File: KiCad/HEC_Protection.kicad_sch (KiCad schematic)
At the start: 11 parts, among them U10 74LS30, U11 74LS32, U17 74LS74, U18 74LS74, U19 74LS30, U22 74LS02, U23 74LS30, U24 74LS74, U25 74LS541, U26 74LS541

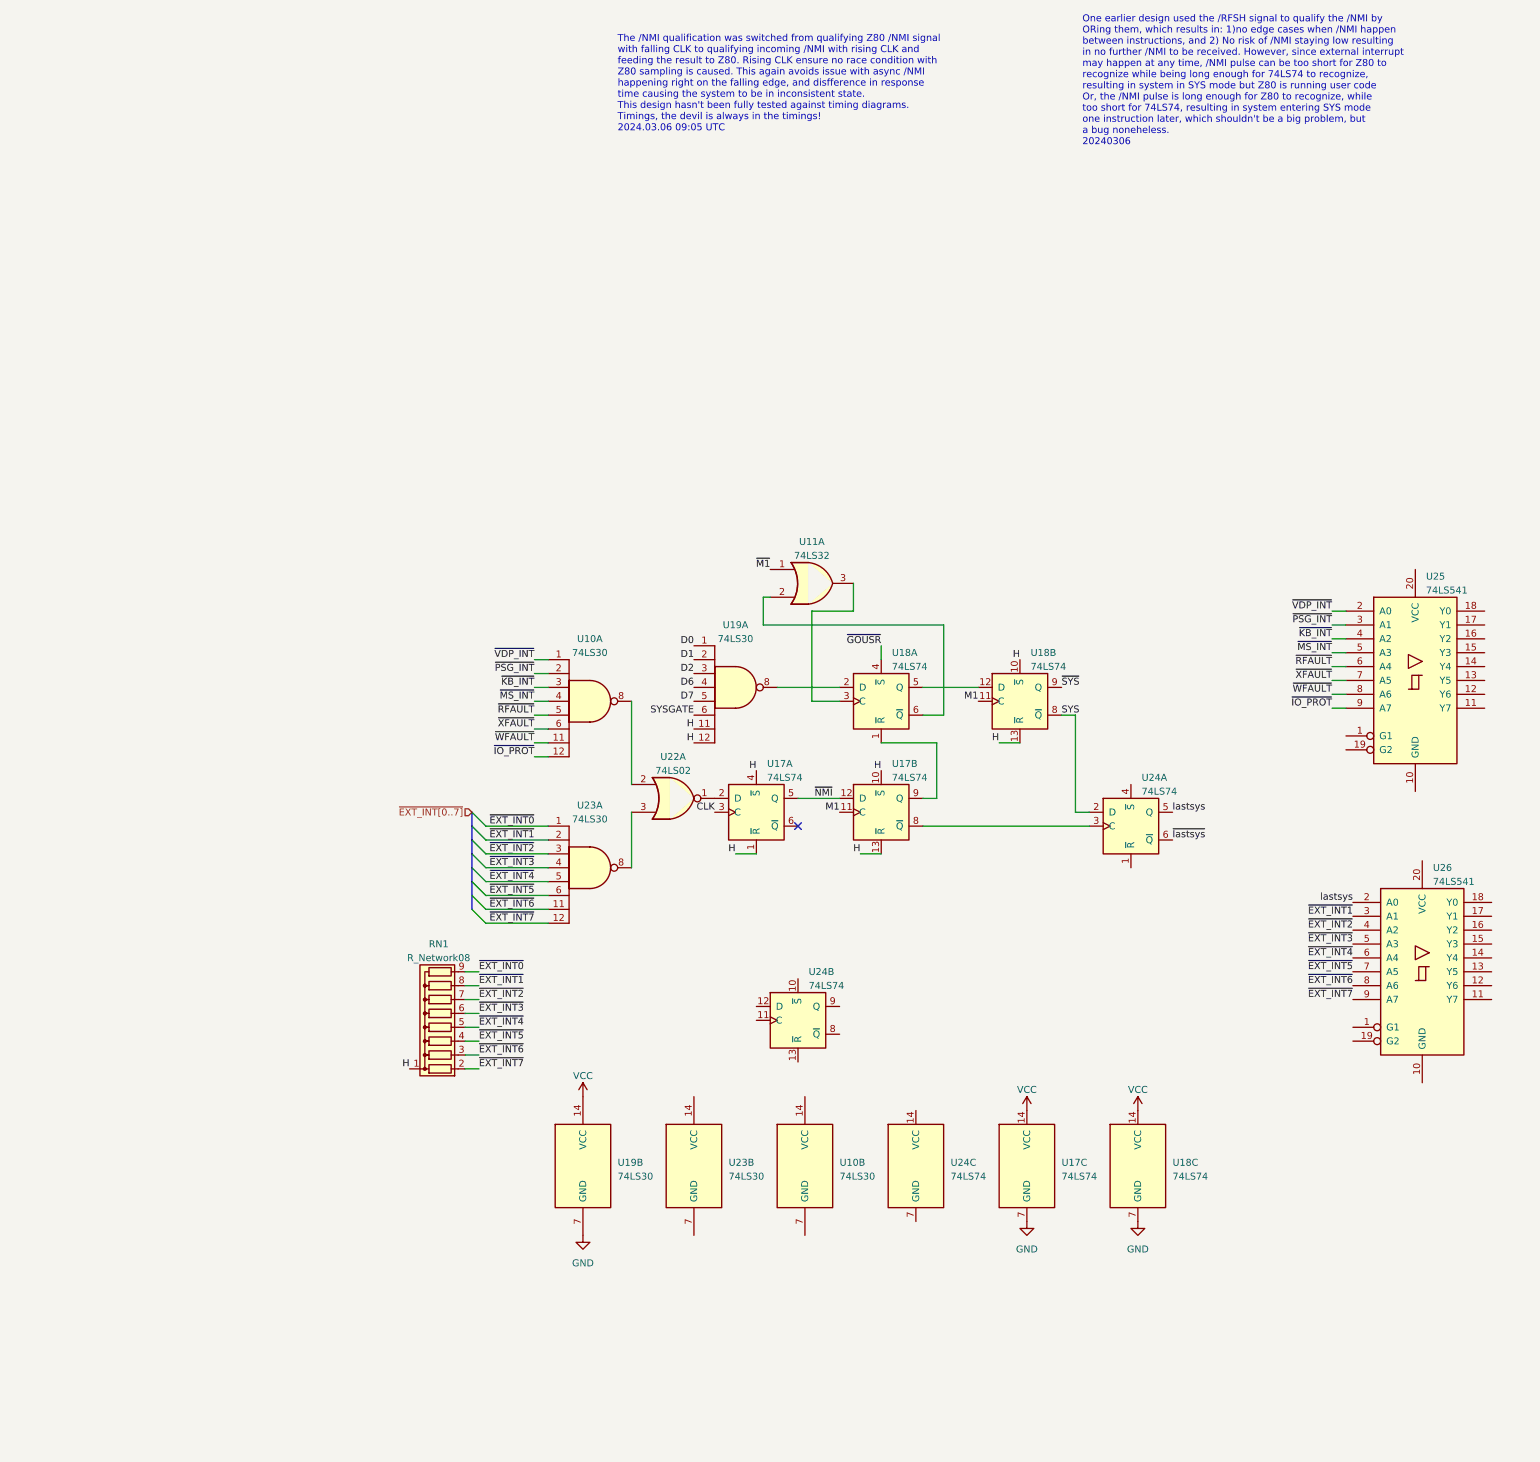
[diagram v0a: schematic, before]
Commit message: Update NMI timing circuit
Updated the NMI generation circuit to prevent a bug occurring when NMI is generated between the rising edge of the last T cycle of an instruction and the falling edge of M1 of the next. Due to delay in M1 signal, the NMI would be qualified one instruction earlier, causing the HEC to enter SYS mode one instruction earlier. If the instruction is an IO instruction by an user program, it can cause a write to any port and potentially destabilize the system.
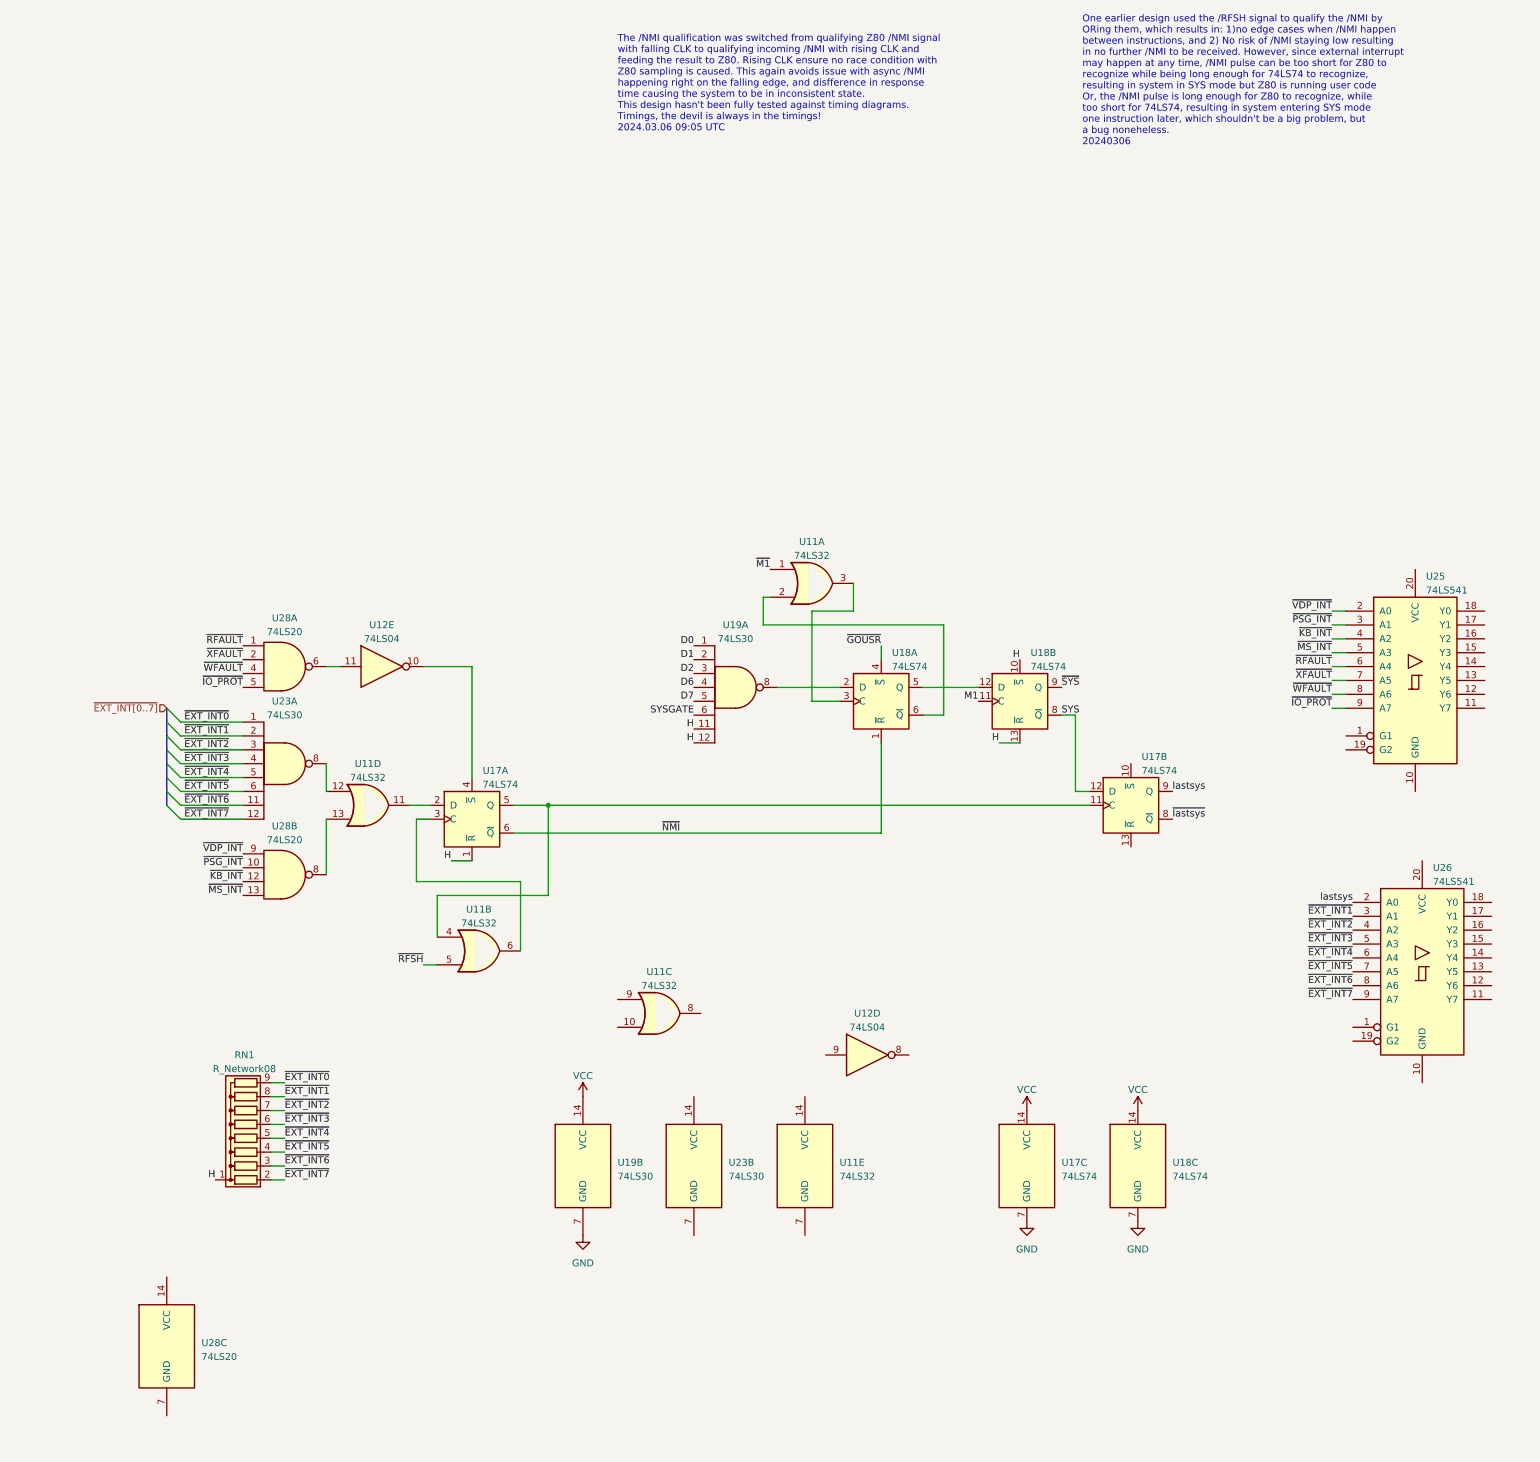
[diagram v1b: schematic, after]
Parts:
- removed U10: 74LS30, Package_DIP:DIP-14_W7.62mm_Socket, symbol 74xx:74LS30
- removed U22: 74LS02, Package_DIP:DIP-14_W7.62mm_Socket, symbol 74xx:74LS02
- removed U24: 74LS74, Package_DIP:DIP-14_W7.62mm_Socket, symbol 74xx:74LS74
- added unit 2 of U11
- added unit 3 of U11
- added unit 4 of U11
- added unit 5 of U11
- added U12: 74LS04, Package_DIP:DIP-14_W7.62mm_Socket, symbol 74xx:74LS04
- added U28: 74LS20, symbol 74xx:74LS20
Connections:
- net H: no longer U17.10 (~{S}), U17.13 (~{R}), U17.4 (~{S})
- net M1: no longer U17.11 (C)
- net SYS: now also U17.12 (D)
- net lastsys: now also U17.9 (Q)
- net ~{IO_PROT}: now also U28.5
- net ~{KB_INT}: now also U28.12
- net ~{MS_INT}: now also U28.13
- net ~{NMI}: now also U17.6 (~{Q}), U18.1 (~{R}); no longer U17.12 (D), U17.5 (Q)
- net ~{PSG_INT}: now also U28.10
- net ~{RFAULT}: now also U28.1
- net ~{VDP_INT}: now also U28.9
- net ~{WFAULT}: now also U28.4
- net ~{XFAULT}: now also U28.2
- net ~{lastsys}: now also U17.8 (~{Q})
- net at U23.8: now also U11.12
- net at U17.2 (D): now also U11.11
- net CLK: no longer names the net of U17.3 (C)
- net CLK: now also U11.6
- new net: U11.4, U17.11 (C), U17.5 (Q)
- new net: U12.10, U17.4 (~{S})
- new net: U12.11, U28.6
- new net: U11.13, U28.8
- new net ~{RFSH}: U11.5
- no-connect marks 1 -> 0
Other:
- moved on the sheet: RN1, U17A, U17B, U23A

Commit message: Add NMI reset circuit
Added a circuit that will reset /NMI state for the HEC and allow further NMI when /INTEN or /GOUSR port is accessed.
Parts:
- added U11: 74LS08, symbol 74xx:74LS08
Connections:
- net H: no longer U17.1 (~{R})
- net ~{GOUSR}: now also U11.1
- new net: U11.3, U17.1 (~{R})
- new net ~{INTEN}: U11.2
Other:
- moved on the sheet: U11A, U19A

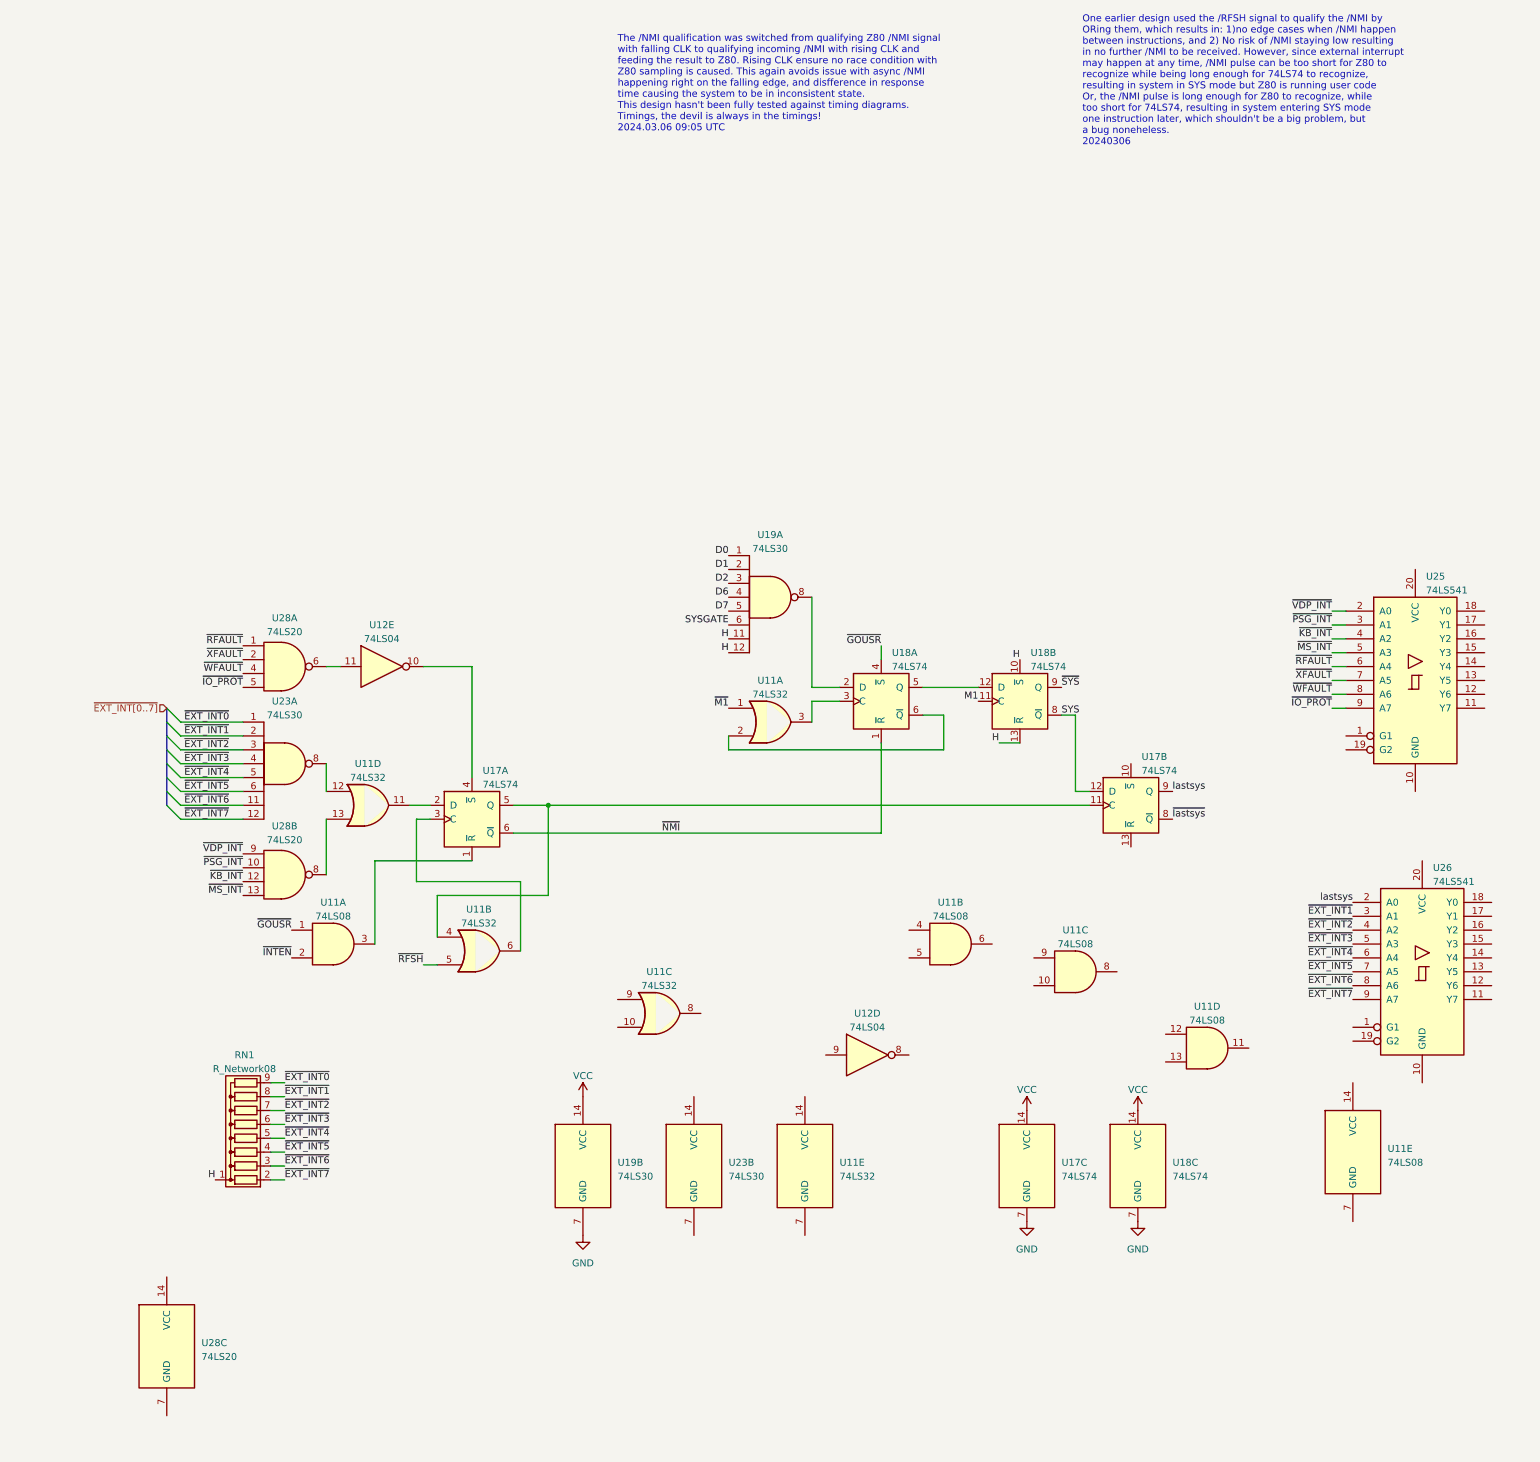
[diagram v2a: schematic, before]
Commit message: Update to protection circuit
Update the protection circuit to prevent all interrupts when HEC is in SYS mode
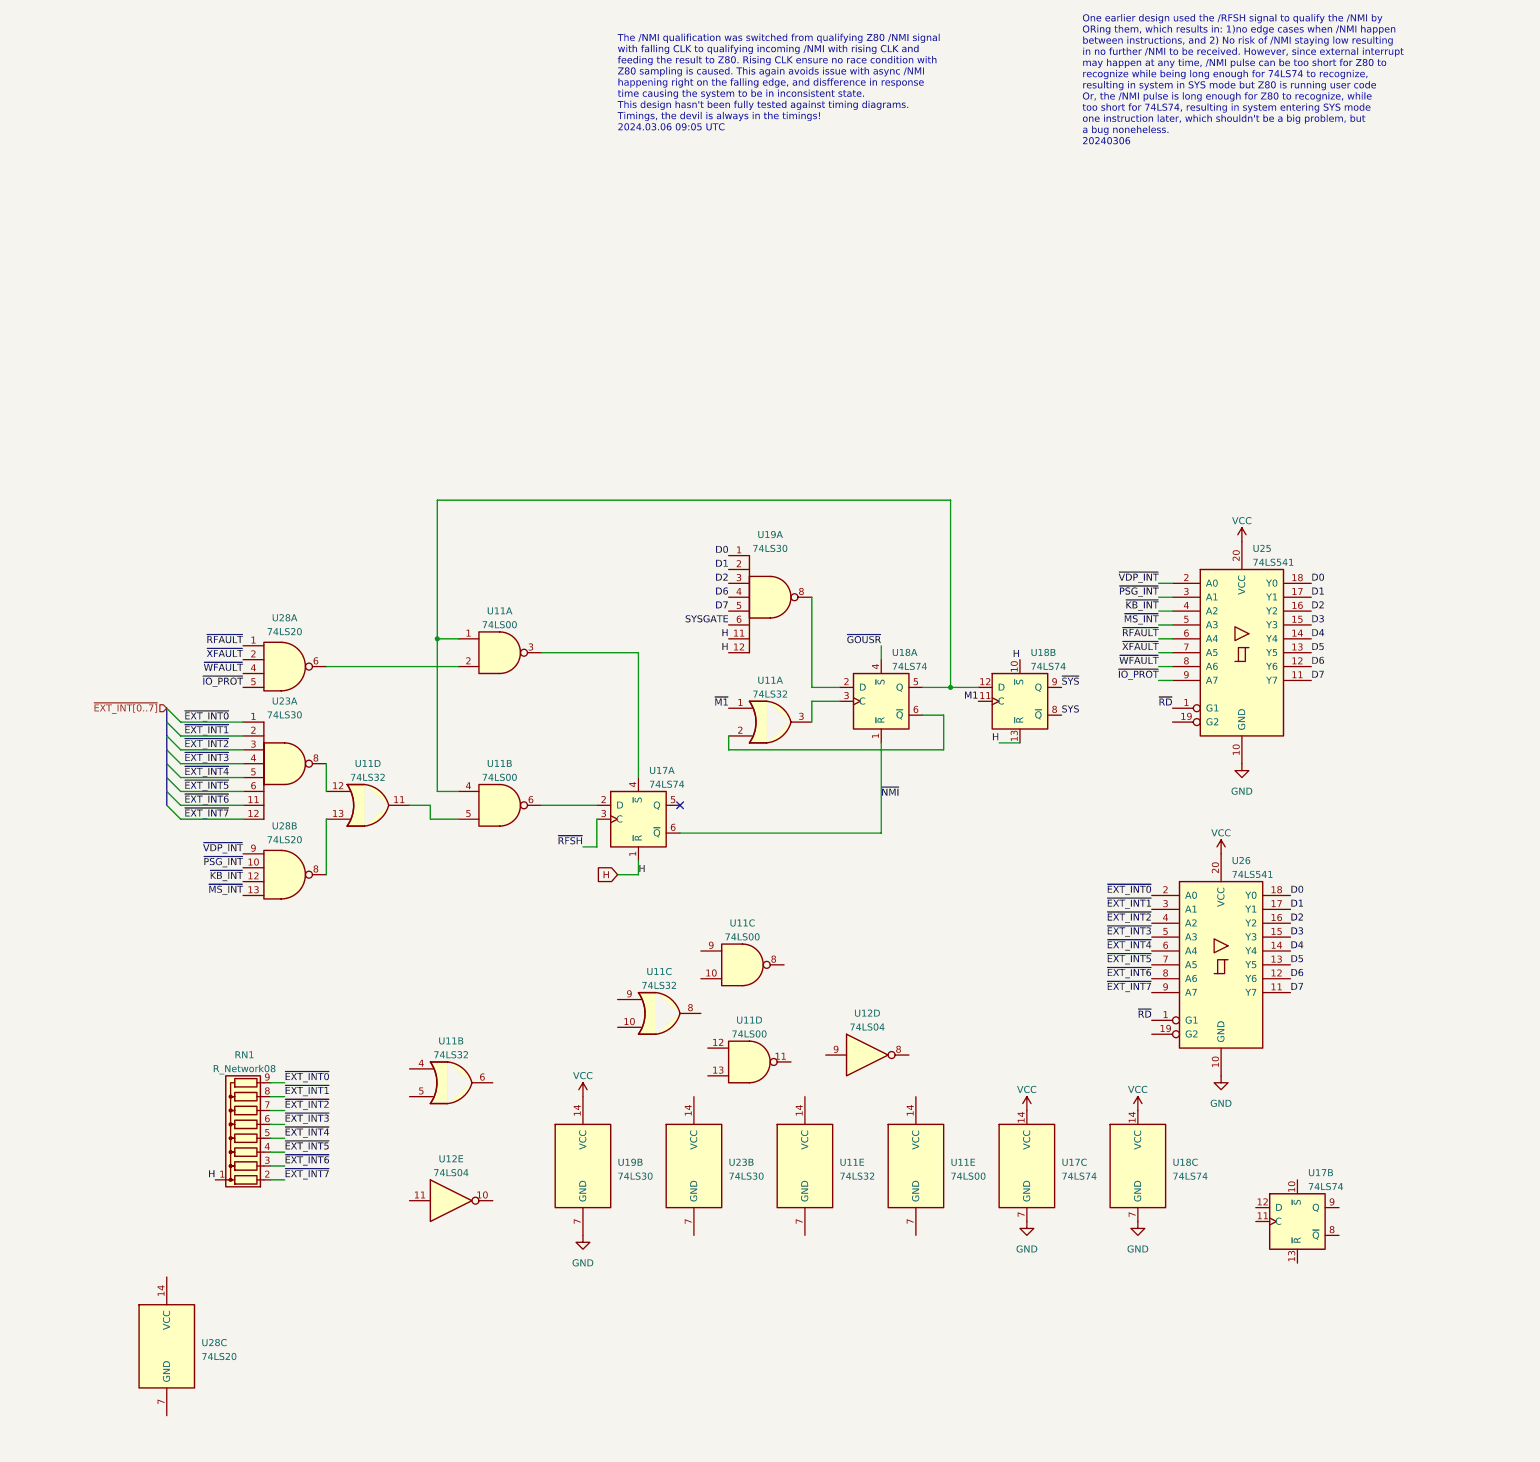
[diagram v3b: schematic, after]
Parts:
- removed U11: 74LS08, symbol 74xx:74LS08
- added U11: 74LS00, symbol 74xx:74LS00
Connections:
- net D0: now also U25.18 (Y0), U26.18 (Y0)
- net D1: now also U25.17 (Y1), U26.17 (Y1)
- net D2: now also U25.16 (Y2), U26.16 (Y2)
- net D6: now also U25.12 (Y6), U26.12 (Y6)
- net D7: now also U25.11 (Y7), U26.11 (Y7)
- net GND: now also U25.10 (GND), U26.10 (GND)
- net H: now also U17.1 (~{R})
- net SYS: no longer U17.12 (D)
- net VCC: now also U25.20 (VCC), U26.20 (VCC)
- net ~{EXT_INT0}: now also U26.2 (A0)
- net ~{RFSH}: now also U17.3 (C); no longer U11.5
- net at U11.6: no longer U17.3 (C)
- net at U12.10: no longer U17.4 (~{S})
- net at U12.11: no longer U28.6
- net ~{RD}: now reaches U25.1 (G1)
- net ~{RD}: now also U26.1 (G1)
- net D5: now reaches U25.13 (Y5)
- net D5: now also U26.13 (Y5)
- net D4: now reaches U25.14 (Y4)
- net D4: now also U26.14 (Y4)
- net D3: now reaches U25.15 (Y3)
- net D3: now also U26.15 (Y3)
- net at U18.12 (D), U18.5 (Q): now also U11.1, U11.4
- net at U17.2 (D): now also U11.6; no longer U11.11
- net lastsys: no longer names the net of U17.9 (Q)
- net lastsys: no longer U26.2 (A0)
- net ~{lastsys}: no longer names the net of U17.8 (~{Q})
- new net: U11.2, U28.6
- new net: U11.3, U17.4 (~{S})
- new net: U11.11, U11.5
- now unconnected: U11.4, U17.11 (C), U17.5 (Q)
- no-connect marks 0 -> 1
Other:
- moved on the sheet: U11B, U12E, U17A, U17B, U25, U26
